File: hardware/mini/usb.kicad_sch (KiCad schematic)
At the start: 27 parts, among them J5 USB_C_Receptacle_USB2.0_16P, Q6 WSD30L60DN56, U10 STUSB4500QTR, U3 TPD2EUSB30

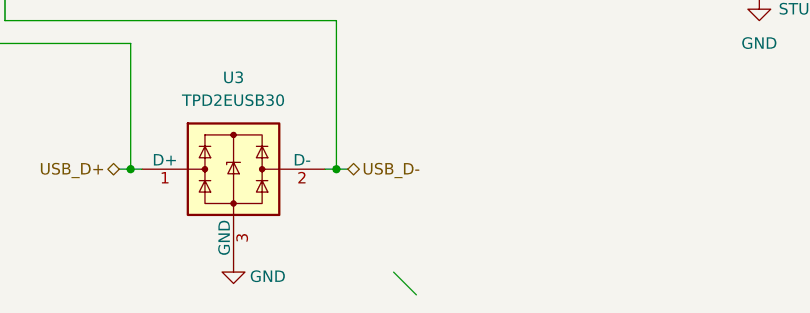
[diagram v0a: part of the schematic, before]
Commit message: route power
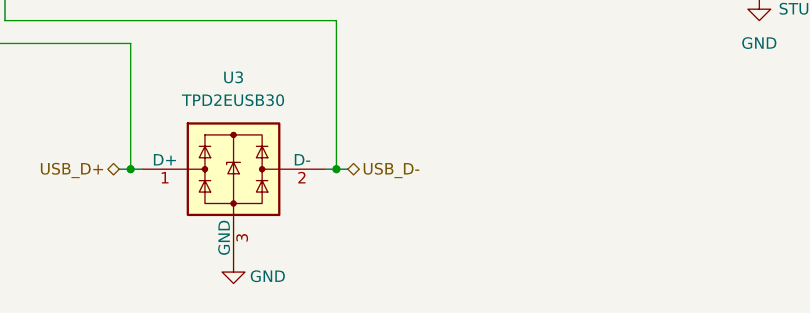
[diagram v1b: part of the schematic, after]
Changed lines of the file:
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@@
 		(at 173.99 104.14)
-	)
-	(bus_entry
-		(at 118.11 148.59)
-		(size 2.54 2.54)
-		(stroke
-			(width 0)
-			(type default)
-		)
 	)
 	(wire

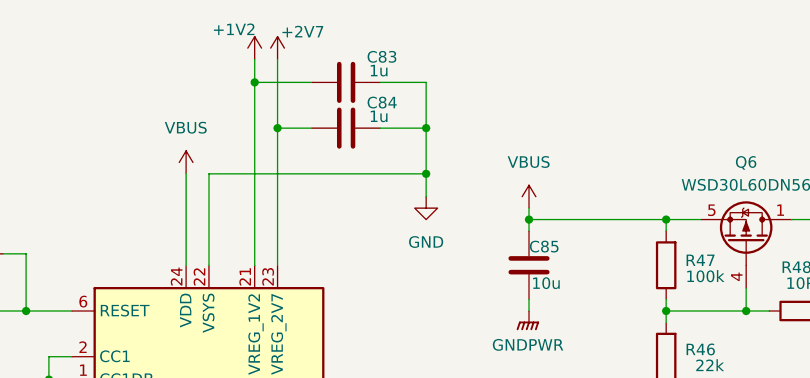
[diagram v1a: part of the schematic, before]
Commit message: reroute all except 3V3 & GND
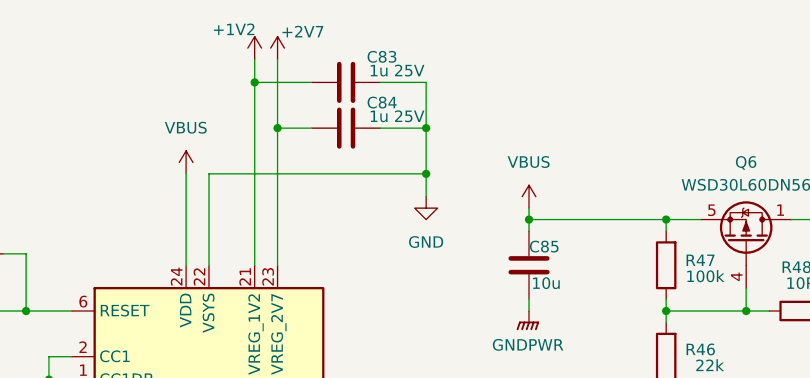
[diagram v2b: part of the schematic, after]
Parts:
- C83, C84: value 1u -> 1u 25V; footprint Capacitor_SMD:C_0603_1608Metric -> Capacitor_SMD:C_0402_1005Metric; LCSC C15849 -> C52923
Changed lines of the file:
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@@
 			)
 		)
-		(property "Value" "1u"
+		(property "Value" "1u 25V"
 			(at 176.53 54.61 90)
 			(effects
@@
 			)
 		)
-		(property "Footprint" "Capacitor_SMD:C_0603_1608Metric"
+		(property "Footprint" "Capacitor_SMD:C_0402_1005Metric"
 			(at 177.8 54.9148 0)
 			(effects
@@
 			)
 		)
-		(property "LCSC" "C15849"
+		(property "LCSC" "C52923"
 			(at 173.99 55.88 0)
 			(effects
@@
 			)
 		)
-		(property "Value" "1u"
+		(property "Value" "1u 25V"
 			(at 176.53 49.53 90)
 			(effects
@@
 			)
 		)
-		(property "Footprint" "Capacitor_SMD:C_0603_1608Metric"
+		(property "Footprint" "Capacitor_SMD:C_0402_1005Metric"
 			(at 177.8 49.8348 0)
 			(effects
@@
 			)
 		)
-		(property "LCSC" "C15849"
+		(property "LCSC" "C52923"
 			(at 173.99 50.8 0)
 			(effects

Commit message: finish routing
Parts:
- removed NT1: NetTie_2, NetTie:NetTie-2_SMD_Pad0.5mm, symbol Device:NetTie_2
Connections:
- net GNDPWR is gone; now on net GND: C85.2, D23.2 (A), D33.2 (A), J5.A1 (GND), J5.A12 (GND), J5.B1 (GND), J5.B12 (GND), J5.S1 (SHIELD), R45.2, R50.2
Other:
- note removed: "Place next to STUB4500 Transfer of power domain into GND from GNDPWR"
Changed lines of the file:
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@@
 	(generator_version "9.0")
 	(paper "A4")
-	(text "Place next to STUB4500\nTransfer of power domain\ninto GND from GNDPWR"
-		(exclude_from_sim no)
-		(at 197.866 143.256 0)
-		(effects
-			(font
-				(size 1.27 1.27)
-			)
-			(justify left)
-		)
-	)
 	(junction
 		(at 209.55 76.2)
@@
 	)
 	(junction
-		(at 91.44 80.01)
-		(diameter 0)
-		(color 0 0 0 0)
-	)
-	(junction
 		(at 209.55 66.04)
 		(diameter 0)
@@
 	(wire
 		(pts
-			(xy 91.44 78.74) (xy 91.44 80.01)
-		)
-		(stroke
-			(width 0)
-			(type default)
-		)
-	)
-	(wire
-		(pts
 			(xy 166.37 48.26) (xy 166.37 55.88)
 		)
@@
 	(wire
 		(pts
-			(xy 204.47 132.08) (xy 201.93 132.08)
+			(xy 201.93 132.08) (xy 212.09 132.08)
 		)
 		(stroke
@@
 		)
 	)
-	(wire
-		(pts
-			(xy 209.55 132.08) (xy 212.09 132.08)
-		)
-		(stroke
-			(width 0)
-			(type default)
-		)
-	)
 	(label "CC2"
 		(at 59.69 87.63 0)
@@
 	)
 	(symbol
-		(lib_id "power:PWR_FLAG")
-		(at 91.44 78.74 0)
-		(mirror y)
-		(unit 1)
-		(exclude_from_sim no)
-		(in_bom yes)
-		(on_board yes)
-		(dnp no)
-		(fields_autoplaced yes)
-		(property "Reference" "#FLG01"
-			(at 91.44 76.835 0)
-			(effects
-				(font
-					(size 1.27 1.27)
-				)
-				(hide yes)
-			)
-		)
-		(property "Value" "PWR_FLAG"
-			(at 91.44 73.66 0)
-			(effects
-				(font
-					(size 1.27 1.27)
-				)
-			)
-		)
-		(property "Footprint" ""
-			(at 91.44 78.74 0)
-			(effects
-				(font
-					(size 1.27 1.27)
-				)
-				(hide yes)
-			)
-		)
-		(property "Datasheet" "~"
-			(at 91.44 78.74 0)
-			(effects
-				(font
-					(size 1.27 1.27)
-				)
-				(hide yes)
-			)
-		)
-		(property "Description" "Special symbol for telling ERC where power comes from"
-			(at 91.44 78.74 0)
-			(effects
-				(font
-					(size 1.27 1.27)
-				)
-				(hide yes)
-			)
-		)
-		(pin "1"
-		)
-		(instances
-			(project ""
-				(path "/5aaaac9a-5acd-4aef-ad51-a6d04aa88705/1cbbc356-180d-474b-929e-739812c8bd10"
-					(reference "#FLG01")
-					(unit 1)
-				)
-			)
-		)
-	)
-	(symbol
 		(lib_id "Device:D_Zener")
 		(at 77.47 80.01 0)
@@
 					(unit 1)
 				)
-			)
-		)
-	)
-	(symbol
-		(lib_id "Device:NetTie_2")
-		(at 207.01 132.08 0)
-		(unit 1)
-		(exclude_from_sim no)
-		(in_bom no)
-		(on_board yes)
-		(dnp no)
-		(property "Reference" "NT1"
-			(at 198.374 127.254 0)
-			(effects
-				(font
-					(size 1.27 1.27)
-				)
-			)
-		)
-		(property "Value" "NetTie_2"
-			(at 198.374 129.794 0)
-			(effects
-				(font
-					(size 1.27 1.27)
-				)
-			)
-		)
-		(property "Footprint" "NetTie:NetTie-2_SMD_Pad0.5mm"
-			(at 207.01 132.08 0)
-			(effects
-				(font
-					(size 1.27 1.27)
-				)
-				(hide yes)
-			)
-		)
-		(property "Datasheet" "~"
-			(at 207.01 132.08 0)
-			(effects
-				(font
-					(size 1.27 1.27)
-				)
-				(hide yes)
-			)
-		)
-		(property "Description" "Net tie, 2 pins"
-			(at 207.01 132.08 0)
-			(effects
-				(font
-					(size 1.27 1.27)
-				)
-				(hide yes)
-			)
-		)
-		(pin "2"
-		)
-		(pin "1"
-		)
-		(instances
-			(project ""
-				(path "/5aaaac9a-5acd-4aef-ad51-a6d04aa88705/1cbbc356-180d-474b-929e-739812c8bd10"
-					(reference "NT1")
-					(unit 1)
-				)

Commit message: cleanup schematic
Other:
- title: (none) -> Protovolt MINI
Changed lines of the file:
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@@
 	(generator_version "9.0")
 	(paper "A4")
+	(title_block
+		(title "Protovolt MINI")
+		(date "2025-06-16")
+		(rev "A")
+		(comment 3 "MINI")
+		(comment 4 "Protovolt")
+	)
 	(junction
 		(at 209.55 76.2)

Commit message: first fab run
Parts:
- R43: LCSC C25905 -> C25744
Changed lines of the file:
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@@
 			)
 		)
-		(property "LCSC" "C25905"
+		(property "LCSC" "C25744"
 			(at 132.08 69.85 90)
 			(effects
